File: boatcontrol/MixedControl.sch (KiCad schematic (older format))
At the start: 12 parts, among them J21 Conn_01x01_Male, J22 Conn_01x01_Male, J23 Conn_02x20_Odd_Even Socket, U15 MCP23017-E/SP

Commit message: Fixed I2C addresses
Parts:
- removed JP16, JP17, JP18: SolderJumper_3_Open, Jumper:SolderJumper-3_P1.3mm_Open_RoundedPad1.0x1.5mm_NumberLabels, symbol Jumper:SolderJumper_3_Open
- added JP16, JP17, JP18: SolderJumper_3_Bridged12, symbol Jumper:SolderJumper_3_Bridged12
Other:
- note added: "I2C Address 0x24"
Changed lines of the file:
@@
 	3250 4450 2950 4450
-$Comp
-L Jumper:SolderJumper_3_Open JP?
-U 1 1 E142CC81
-P 2950 4300
-AR Path="/E142CC81" Ref="JP?"  Part="1"
-AR Path="/D16552B4/E142CC81" Ref="JP?"  Part="1"
-AR Path="/D1BB8DB4/E142CC81" Ref="JP?"  Part="1"
-AR Path="/E0EE2714/E1383403/E142CC81" Ref="JP?"  Part="1"
-AR Path="/E171B33C/E142CC81" Ref="JP18"  Part="1"
-F 0 "JP18" H 2950 4400 50  0000 C CNN
-F 1 "SolderJumper_3_Open" V 2800 4750 50  0001 C CNN
-F 2 "Jumper:SolderJumper-3_P1.3mm_Open_RoundedPad1.0x1.5mm_NumberLabels" H 2950 4300 50  0001 C CNN
-F 3 "~" H 2950 4300 50  0001 C CNN
-	1    2950 4300
-	1    0    0    -1
-$EndComp
-$Comp
-L Jumper:SolderJumper_3_Open JP?
-U 1 1 E142CC87
-P 2400 4400
-AR Path="/E142CC87" Ref="JP?"  Part="1"
-AR Path="/D16552B4/E142CC87" Ref="JP?"  Part="1"
-AR Path="/D1BB8DB4/E142CC87" Ref="JP?"  Part="1"
-AR Path="/E0EE2714/E1383403/E142CC87" Ref="JP?"  Part="1"
-AR Path="/E171B33C/E142CC87" Ref="JP17"  Part="1"
-F 0 "JP17" H 2400 4500 50  0000 C CNN
-F 1 "SolderJumper_3_Open" V 2250 4850 50  0001 C CNN
-F 2 "Jumper:SolderJumper-3_P1.3mm_Open_RoundedPad1.0x1.5mm_NumberLabels" H 2400 4400 50  0001 C CNN
-F 3 "~" H 2400 4400 50  0001 C CNN
-	1    2400 4400
-	1    0    0    -1
-$EndComp
-$Comp
-L Jumper:SolderJumper_3_Open JP?
-U 1 1 E142CC8D
-P 1900 4500
-AR Path="/E142CC8D" Ref="JP?"  Part="1"
-AR Path="/D16552B4/E142CC8D" Ref="JP?"  Part="1"
-AR Path="/D1BB8DB4/E142CC8D" Ref="JP?"  Part="1"
-AR Path="/E0EE2714/E1383403/E142CC8D" Ref="JP?"  Part="1"
-AR Path="/E171B33C/E142CC8D" Ref="JP16"  Part="1"
-F 0 "JP16" H 1900 4600 50  0000 C CNN
-F 1 "SolderJumper_3_Open" V 1750 4950 50  0001 C CNN
-F 2 "Jumper:SolderJumper-3_P1.3mm_Open_RoundedPad1.0x1.5mm_NumberLabels" H 1900 4500 50  0001 C CNN
-F 3 "~" H 1900 4500 50  0001 C CNN
-	1    1900 4500
-	1    0    0    -1
-$EndComp
 $Comp
 L Connector:Conn_01x01_Male J?
@@
 Wire Wire Line
 	2600 4950 3150 4950
-Wire Wire Line
-	1700 2750 1700 4500
 Wire Wire Line
 	2100 4500 2100 4950
@@
 Wire Wire Line
 	3250 3950 3100 3950
-Connection ~ 3050 4100
+Text Notes 3700 4050 3    50   ~ 0
+I2C Address 0x24
+$Comp
+L Jumper:SolderJumper_3_Bridged12 JP?
+U 1 1 5F735A80
+P 2950 4300
+AR Path="/5F735A80" Ref="JP?"  Part="1"
+AR Path="/D16552B4/5F735A80" Ref="JP?"  Part="1"
+AR Path="/E171B33C/5F735A80" Ref="JP18"  Part="1"
+F 0 "JP18" H 2950 4413 50  0000 C CNN
+F 1 "SolderJumper_3_Bridged12" H 2950 4414 50  0001 C CNN
+F 2 "" H 2950 4300 50  0001 C CNN
+F 3 "~" H 2950 4300 50  0001 C CNN
+	1    2950 4300
+	1    0    0    -1
+$EndComp
+$Comp
+L Jumper:SolderJumper_3_Bridged12 JP?
+U 1 1 5F735A8C
+P 1900 4500
+AR Path="/5F735A8C" Ref="JP?"  Part="1"
+AR Path="/D16552B4/5F735A8C" Ref="JP?"  Part="1"
+AR Path="/E171B33C/5F735A8C" Ref="JP16"  Part="1"
+F 0 "JP16" H 1900 4613 50  0000 C CNN
+F 1 "SolderJumper_3_Bridged12" H 1900 4614 50  0001 C CNN
+F 2 "" H 1900 4500 50  0001 C CNN
+F 3 "~" H 1900 4500 50  0001 C CNN
+	1    1900 4500
+	-1   0    0    -1
+$EndComp
+$Comp
+L Jumper:SolderJumper_3_Bridged12 JP?
+U 1 1 5F74DFEC
+P 2400 4400
+AR Path="/5F74DFEC" Ref="JP?"  Part="1"
+AR Path="/D16552B4/5F74DFEC" Ref="JP?"  Part="1"
+AR Path="/E171B33C/5F74DFEC" Ref="JP17"  Part="1"
+F 0 "JP17" H 2400 4513 50  0000 C CNN
+F 1 "SolderJumper_3_Bridged12" H 2400 4514 50  0001 C CNN
+F 2 "" H 2400 4400 50  0001 C CNN
+F 3 "~" H 2400 4400 50  0001 C CNN
+	1    2400 4400
+	-1   0    0    -1
+$EndComp
+Wire Wire Line
+	1700 2750 1700 4500
 $EndSCHEMATC

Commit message: Fixed SolderJumpers
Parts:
- JP16, JP17, JP18: footprint (none) -> Jumper:SolderJumper-3_P1.3mm_Bridged12_RoundedPad1.0x1.5mm; symbol Jumper:SolderJumper_3_Bridged12 -> Jumper:SolderJumper_3_Bridged12_Output
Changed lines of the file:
@@
 I2C Address 0x24
 $Comp
-L Jumper:SolderJumper_3_Bridged12 JP?
+L Jumper:SolderJumper_3_Bridged12_Output JP?
 U 1 1 5F735A80
 P 2950 4300
@@
 F 0 "JP18" H 2950 4413 50  0000 C CNN
 F 1 "SolderJumper_3_Bridged12" H 2950 4414 50  0001 C CNN
-F 2 "" H 2950 4300 50  0001 C CNN
+F 2 "Jumper:SolderJumper-3_P1.3mm_Bridged12_RoundedPad1.0x1.5mm" H 2950 4300 50  0001 C CNN
 F 3 "~" H 2950 4300 50  0001 C CNN
 	1    2950 4300
@@
 $EndComp
 $Comp
-L Jumper:SolderJumper_3_Bridged12 JP?
+L Jumper:SolderJumper_3_Bridged12_Output JP?
 U 1 1 5F735A8C
 P 1900 4500
@@
 F 0 "JP16" H 1900 4613 50  0000 C CNN
 F 1 "SolderJumper_3_Bridged12" H 1900 4614 50  0001 C CNN
-F 2 "" H 1900 4500 50  0001 C CNN
+F 2 "Jumper:SolderJumper-3_P1.3mm_Bridged12_RoundedPad1.0x1.5mm" H 1900 4500 50  0001 C CNN
 F 3 "~" H 1900 4500 50  0001 C CNN
 	1    1900 4500
@@
 $EndComp
 $Comp
-L Jumper:SolderJumper_3_Bridged12 JP?
+L Jumper:SolderJumper_3_Bridged12_Output JP?
 U 1 1 5F74DFEC
 P 2400 4400
@@
 F 0 "JP17" H 2400 4513 50  0000 C CNN
 F 1 "SolderJumper_3_Bridged12" H 2400 4514 50  0001 C CNN
-F 2 "" H 2400 4400 50  0001 C CNN
+F 2 "Jumper:SolderJumper-3_P1.3mm_Bridged12_RoundedPad1.0x1.5mm" H 2400 4400 50  0001 C CNN
 F 3 "~" H 2400 4400 50  0001 C CNN
 	1    2400 4400

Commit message: Before starting the PCB fresh
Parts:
- renumbered H27 to H2401, H28 to H2402, H29 to H2403, H30 to H2404, J21 to J2401, J22 to J2402, J23 to J2403, JP16 to JP2401, JP17 to JP2402, JP18 to JP2403, JP19 to JP2404, U15 to U2401
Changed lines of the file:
@@
 AR Path="/D1BB8DB4/E142CB7C" Ref="U?"  Part="1"
 AR Path="/E0EE2714/E1383403/E142CB7C" Ref="U?"  Part="1"
-AR Path="/E171B33C/E142CB7C" Ref="U15"  Part="1"
-F 0 "U15" V 4000 3750 50  0000 L CNN
+AR Path="/E171B33C/E142CB7C" Ref="U2401"  Part="1"
+F 0 "U2401" V 4000 3750 50  0000 L CNN
 F 1 "MCP23017-E/SP" V 3900 3550 50  0000 L CNN
 F 2 "Package_DIP:DIP-28_W7.62mm" H 4150 2850 50  0001 L CNN
@@
 AR Path="/D1BB8DB4/E142CC74" Ref="JP?"  Part="1"
 AR Path="/E0EE2714/E1383403/E142CC74" Ref="JP?"  Part="1"
-AR Path="/E171B33C/E142CC74" Ref="JP19"  Part="1"
-F 0 "JP19" H 3000 4050 50  0000 C CNN
+AR Path="/E171B33C/E142CC74" Ref="JP2404"  Part="1"
+F 0 "JP2404" H 3000 4050 50  0000 C CNN
 F 1 "Jumper_NO_Small" H 3050 3850 50  0001 C CNN
 F 2 "Connector_PinHeader_2.54mm:PinHeader_1x02_P2.54mm_Vertical" H 3000 3950 50  0001 C CNN
@@
 AR Path="/D1BB8DB4/E142CC7A" Ref="J?"  Part="1"
 AR Path="/E0EE2714/E1383403/E142CC7A" Ref="J?"  Part="1"
-AR Path="/E171B33C/E142CC7A" Ref="J22"  Part="1"
-F 0 "J22" H 2950 3800 50  0000 R CNN
+AR Path="/E171B33C/E142CC7A" Ref="J2402"  Part="1"
+F 0 "J2402" H 2950 3800 50  0000 R CNN
 F 1 "Conn_01x01_Male" H 2872 3773 50  0001 R CNN
 F 2 "Connector_PinHeader_2.54mm:PinHeader_1x01_P2.54mm_Vertical" H 2900 3750 50  0001 C CNN
@@
 AR Path="/D1BB8DB4/E142CC93" Ref="J?"  Part="1"
 AR Path="/E0EE2714/E1383403/E142CC93" Ref="J?"  Part="1"
-AR Path="/E171B33C/E142CC93" Ref="J21"  Part="1"
-F 0 "J21" H 2950 3700 50  0000 R CNN
+AR Path="/E171B33C/E142CC93" Ref="J2401"  Part="1"
+F 0 "J2401" H 2950 3700 50  0000 R CNN
 F 1 "Conn_01x01_Male" H 2872 3673 50  0001 R CNN
 F 2 "Connector_PinHeader_2.54mm:PinHeader_1x01_P2.54mm_Vertical" H 2900 3650 50  0001 C CNN
@@
 AR Path="/D1BB8DB4/E142CCB8" Ref="#PWR?"  Part="1"
 AR Path="/E0EE2714/E1383403/E142CCB8" Ref="#PWR?"  Part="1"
-AR Path="/E171B33C/E142CCB8" Ref="#PWR081"  Part="1"
-F 0 "#PWR081" H 3950 4700 50  0001 C CNN
+AR Path="/E171B33C/E142CCB8" Ref="#PWR02402"  Part="1"
+F 0 "#PWR02402" H 3950 4700 50  0001 C CNN
 F 1 "GND" H 4100 4900 50  0000 C CNN
 F 2 "" H 3950 4950 50  0001 C CNN
@@
 AR Path="/D1BB8DB4/E142CCC5" Ref="#PWR?"  Part="1"
 AR Path="/E0EE2714/E1383403/E142CCC5" Ref="#PWR?"  Part="1"
-AR Path="/E171B33C/E142CCC5" Ref="#PWR080"  Part="1"
-F 0 "#PWR080" H 3950 2600 50  0001 C CNN
+AR Path="/E171B33C/E142CCC5" Ref="#PWR02401"  Part="1"
+F 0 "#PWR02401" H 3950 2600 50  0001 C CNN
 F 1 "+5V" H 4100 2800 50  0000 C CNN
 F 2 "" H 3950 2750 50  0001 C CNN
@@
 AR Path="/E0EE2714/E15696A6" Ref="H?"  Part="1"
 AR Path="/E0EE2714/E1383403/E15696A6" Ref="H?"  Part="1"
-AR Path="/E171B33C/E15696A6" Ref="H29"  Part="1"
-F 0 "H29" H 9700 3800 50  0000 L CNN
+AR Path="/E171B33C/E15696A6" Ref="H2403"  Part="1"
+F 0 "H2403" H 9700 3800 50  0000 L CNN
 F 1 "MountingHole" V 9750 3750 50  0001 L CNN
 F 2 "MountingHole:MountingHole_3mm" H 9750 3650 50  0001 C CNN
@@
 AR Path="/E0EE2714/E15696A0" Ref="H?"  Part="1"
 AR Path="/E0EE2714/E1383403/E15696A0" Ref="H?"  Part="1"
-AR Path="/E171B33C/E15696A0" Ref="H30"  Part="1"
-F 0 "H30" H 9700 3850 50  0000 L CNN
+AR Path="/E171B33C/E15696A0" Ref="H2404"  Part="1"
+F 0 "H2404" H 9700 3850 50  0000 L CNN
 F 1 "MountingHole" H 9850 3955 50  0001 L CNN
 F 2 "MountingHole:MountingHole_3mm" H 9750 4000 50  0001 C CNN
@@
 AR Path="/E0EE2714/E156969A" Ref="J?"  Part="1"
 AR Path="/E0EE2714/E1383403/E156969A" Ref="J?"  Part="1"
-AR Path="/E171B33C/E156969A" Ref="J23"  Part="1"
-F 0 "J23" V 8600 4900 50  0000 R CNN
+AR Path="/E171B33C/E156969A" Ref="J2403"  Part="1"
+F 0 "J2403" V 8600 4900 50  0000 R CNN
 F 1 "Conn_02x20_Odd_Even Socket" V 8600 4200 50  0000 R CNN
 F 2 "Connector_PinHeader_2.54mm:PinHeader_2x20_P2.54mm_Vertical" H 8550 3800 50  0001 C CNN
@@
 AR Path="/E0EE2714/E15696AC" Ref="H?"  Part="1"
 AR Path="/E0EE2714/E1383403/E15696AC" Ref="H?"  Part="1"
-AR Path="/E171B33C/E15696AC" Ref="H27"  Part="1"
-F 0 "H27" V 7600 3600 50  0000 L CNN
+AR Path="/E171B33C/E15696AC" Ref="H2401"  Part="1"
+F 0 "H2401" V 7600 3600 50  0000 L CNN
 F 1 "MountingHole" H 7550 3605 50  0001 L CNN
 F 2 "MountingHole:MountingHole_3mm" H 7450 3650 50  0001 C CNN
@@
 AR Path="/E0EE2714/E15696B2" Ref="H?"  Part="1"
 AR Path="/E0EE2714/E1383403/E15696B2" Ref="H?"  Part="1"
-AR Path="/E171B33C/E15696B2" Ref="H28"  Part="1"
-F 0 "H28" V 7300 3950 50  0000 L CNN
+AR Path="/E171B33C/E15696B2" Ref="H2402"  Part="1"
+F 0 "H2402" V 7300 3950 50  0000 L CNN
 F 1 "MountingHole" H 7550 3955 50  0001 L CNN
 F 2 "MountingHole:MountingHole_3mm" H 7450 4000 50  0001 C CNN
@@
 P 9650 3850
 AR Path="/E0EE2714/E1383403/E16C27B4" Ref="#PWR?"  Part="1"
-AR Path="/E171B33C/E16C27B4" Ref="#PWR082"  Part="1"
-F 0 "#PWR082" H 9650 3600 50  0001 C CNN
+AR Path="/E171B33C/E16C27B4" Ref="#PWR02403"  Part="1"
+F 0 "#PWR02403" H 9650 3600 50  0001 C CNN
 F 1 "GND" V 9650 3750 50  0000 R CNN
 F 2 "" H 9650 3850 50  0001 C CNN
@@
 AR Path="/5F735A80" Ref="JP?"  Part="1"
 AR Path="/D16552B4/5F735A80" Ref="JP?"  Part="1"
-AR Path="/E171B33C/5F735A80" Ref="JP18"  Part="1"
-F 0 "JP18" H 2950 4413 50  0000 C CNN
+AR Path="/E171B33C/5F735A80" Ref="JP2403"  Part="1"
+F 0 "JP2403" H 2950 4413 50  0000 C CNN
 F 1 "SolderJumper_3_Bridged12" H 2950 4414 50  0001 C CNN
 F 2 "Jumper:SolderJumper-3_P1.3mm_Bridged12_RoundedPad1.0x1.5mm" H 2950 4300 50  0001 C CNN
@@
 AR Path="/5F735A8C" Ref="JP?"  Part="1"
 AR Path="/D16552B4/5F735A8C" Ref="JP?"  Part="1"
-AR Path="/E171B33C/5F735A8C" Ref="JP16"  Part="1"
-F 0 "JP16" H 1900 4613 50  0000 C CNN
+AR Path="/E171B33C/5F735A8C" Ref="JP2401"  Part="1"
+F 0 "JP2401" H 1900 4613 50  0000 C CNN
 F 1 "SolderJumper_3_Bridged12" H 1900 4614 50  0001 C CNN
 F 2 "Jumper:SolderJumper-3_P1.3mm_Bridged12_RoundedPad1.0x1.5mm" H 1900 4500 50  0001 C CNN
@@
 AR Path="/5F74DFEC" Ref="JP?"  Part="1"
 AR Path="/D16552B4/5F74DFEC" Ref="JP?"  Part="1"
-AR Path="/E171B33C/5F74DFEC" Ref="JP17"  Part="1"
-F 0 "JP17" H 2400 4513 50  0000 C CNN
+AR Path="/E171B33C/5F74DFEC" Ref="JP2402"  Part="1"
+F 0 "JP2402" H 2400 4513 50  0000 C CNN
 F 1 "SolderJumper_3_Bridged12" H 2400 4514 50  0001 C CNN
 F 2 "Jumper:SolderJumper-3_P1.3mm_Bridged12_RoundedPad1.0x1.5mm" H 2400 4400 50  0001 C CNN

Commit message: Structured
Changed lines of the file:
@@
 $Descr A4 11693 8268
 encoding utf-8
-Sheet 24 55
+Sheet 23 55
 Title "Boat Control Hat"
 Date "2020-07-09"
@@
 Wire Wire Line
 	1700 2750 1700 4500
+$Sheet
+S 5650 3750 1350 150
+U 5F80BAC6
+F0 "Relay Board" 50
+F1 "RelayBoard.sch" 50
+$EndSheet
 $EndSCHEMATC

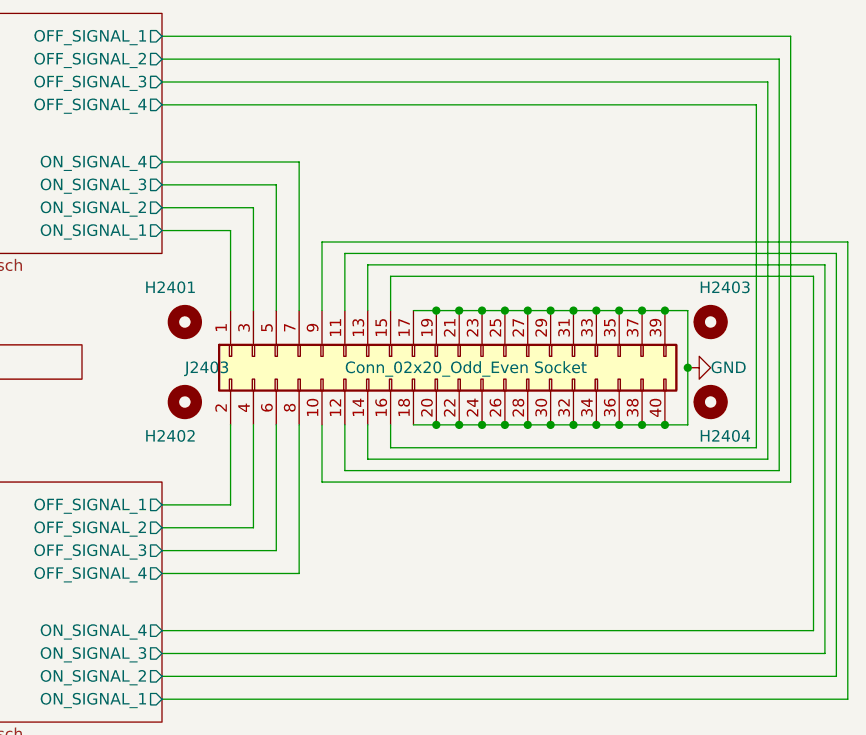
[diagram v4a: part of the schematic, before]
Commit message: Fixed daughter board
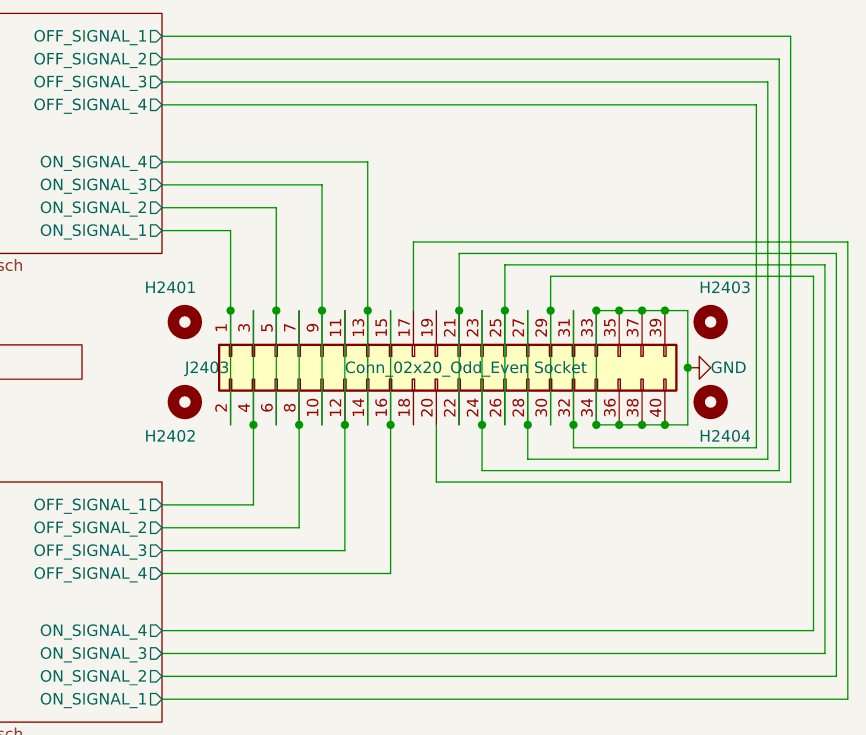
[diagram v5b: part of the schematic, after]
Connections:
- net GND: no longer J2403.17 (Pin_17), J2403.18 (Pin_18), J2403.19 (Pin_19), J2403.20 (Pin_20), J2403.21 (Pin_21), J2403.22 (Pin_22), J2403.23 (Pin_23), J2403.24 (Pin_24), J2403.25 (Pin_25), J2403.26 (Pin_26), J2403.27 (Pin_27), J2403.28 (Pin_28), J2403.29 (Pin_29), J2403.30 (Pin_30), J2403.31 (Pin_31), J2403.32 (Pin_32)
- net MixedBlock1/OFF_SIGNAL_1: now also J2403.20 (Pin_20); no longer J2403.10 (Pin_10)
- net MixedBlock1/OFF_SIGNAL_2: now also J2403.23 (Pin_23), J2403.24 (Pin_24); no longer J2403.12 (Pin_12)
- net MixedBlock1/OFF_SIGNAL_3: now also J2403.27 (Pin_27), J2403.28 (Pin_28); no longer J2403.14 (Pin_14)
- net MixedBlock1/OFF_SIGNAL_4: now also J2403.31 (Pin_31), J2403.32 (Pin_32); no longer J2403.16 (Pin_16)
- net MixedBlock1/ON_SIGNAL_1: now also J2403.2 (Pin_2)
- net MixedBlock1/ON_SIGNAL_2: now also J2403.5 (Pin_5), J2403.6 (Pin_6); no longer J2403.3 (Pin_3)
- net MixedBlock1/ON_SIGNAL_3: now also J2403.10 (Pin_10), J2403.9 (Pin_9); no longer J2403.5 (Pin_5)
- net MixedBlock1/ON_SIGNAL_4: now also J2403.13 (Pin_13), J2403.14 (Pin_14); no longer J2403.7 (Pin_7)
- net MixedBlock2/OFF_SIGNAL_1: now also J2403.3 (Pin_3), J2403.4 (Pin_4); no longer J2403.2 (Pin_2)
- net MixedBlock2/OFF_SIGNAL_2: now also J2403.7 (Pin_7), J2403.8 (Pin_8); no longer J2403.4 (Pin_4)
- net MixedBlock2/OFF_SIGNAL_3: now also J2403.11 (Pin_11), J2403.12 (Pin_12); no longer J2403.6 (Pin_6)
- net MixedBlock2/OFF_SIGNAL_4: now also J2403.15 (Pin_15), J2403.16 (Pin_16); no longer J2403.8 (Pin_8)
- net MixedBlock2/ON_SIGNAL_1: now also J2403.17 (Pin_17); no longer J2403.9 (Pin_9)
- net MixedBlock2/ON_SIGNAL_2: now also J2403.21 (Pin_21), J2403.22 (Pin_22); no longer J2403.11 (Pin_11)
- net MixedBlock2/ON_SIGNAL_3: now also J2403.25 (Pin_25), J2403.26 (Pin_26); no longer J2403.13 (Pin_13)
- net MixedBlock2/ON_SIGNAL_4: now also J2403.29 (Pin_29), J2403.30 (Pin_30); no longer J2403.15 (Pin_15)
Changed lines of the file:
@@
 	4650 4650 4650 5300
 Wire Wire Line
-	8350 4200 8350 4100
-Wire Wire Line
-	8250 4250 8250 4100
-Wire Wire Line
-	8150 4300 8150 4100
-Wire Wire Line
-	8050 4350 8050 4100
-Wire Wire Line
-	8350 3600 8350 3450
-Wire Wire Line
-	7350 2950 7950 2950
-Wire Wire Line
-	7950 2950 7950 3600
-Wire Wire Line
-	7350 3050 7850 3050
-Wire Wire Line
-	7850 3050 7850 3600
-Wire Wire Line
-	7350 3150 7750 3150
-Wire Wire Line
-	7750 3150 7750 3600
-Wire Wire Line
 	7650 3250 7650 3600
 Wire Wire Line
 	7350 3250 7650 3250
 Wire Wire Line
-	8250 3400 8250 3600
-Wire Wire Line
-	8150 3350 8150 3600
-Wire Wire Line
-	8050 3300 8050 3600
-Wire Wire Line
-	7350 4750 7950 4750
-Wire Wire Line
-	7950 4750 7950 4100
-Wire Wire Line
-	7350 4650 7850 4650
-Wire Wire Line
-	7850 4650 7850 4100
-Wire Wire Line
-	7350 4550 7750 4550
-Wire Wire Line
-	7750 4550 7750 4100
-Wire Wire Line
-	7350 4450 7650 4450
-Wire Wire Line
-	7650 4450 7650 4100
-Wire Wire Line
-	8450 3600 8550 3600
-Connection ~ 8550 3600
-Wire Wire Line
-	8550 3600 8650 3600
-Connection ~ 8650 3600
-Wire Wire Line
-	8650 3600 8750 3600
-Connection ~ 8750 3600
-Wire Wire Line
-	8750 3600 8850 3600
-Connection ~ 8850 3600
-Wire Wire Line
-	8850 3600 8950 3600
-Connection ~ 8950 3600
-Wire Wire Line
-	8950 3600 9050 3600
-Connection ~ 9050 3600
-Wire Wire Line
-	9050 3600 9150 3600
-Connection ~ 9150 3600
-Wire Wire Line
-	9150 3600 9250 3600
-Connection ~ 9250 3600
-Wire Wire Line
-	9250 3600 9350 3600
-Connection ~ 9350 3600
-Wire Wire Line
-	9350 3600 9450 3600
-Connection ~ 9450 3600
-Wire Wire Line
-	9450 3600 9550 3600
-Wire Wire Line
-	8550 4100 8650 4100
-Connection ~ 8650 4100
-Wire Wire Line
-	8650 4100 8750 4100
-Connection ~ 8750 4100
-Wire Wire Line
-	8750 4100 8850 4100
-Connection ~ 8850 4100
-Wire Wire Line
-	8850 4100 8950 4100
-Connection ~ 8950 4100
-Wire Wire Line
-	8950 4100 9050 4100
-Connection ~ 9050 4100
-Wire Wire Line
-	9050 4100 9150 4100
-Connection ~ 9150 4100
-Wire Wire Line
-	9150 4100 9250 4100
-Connection ~ 9250 4100
-Wire Wire Line
-	9250 4100 9350 4100
-Connection ~ 9350 4100
-Wire Wire Line
-	9350 4100 9450 4100
-Connection ~ 9450 4100
-Wire Wire Line
-	9450 4100 9550 4100
-Connection ~ 9550 3600
-Wire Wire Line
 	9650 3600 9650 3850
-Wire Wire Line
-	9650 4100 9550 4100
-Connection ~ 9550 4100
-Wire Wire Line
-	9550 3600 9650 3600
 $Comp
 L power:GND #PWR?
@@
 	10350 3300 10350 5300
 Wire Wire Line
-	8050 3300 10350 3300
-Wire Wire Line
 	7350 5300 10350 5300
 Wire Wire Line
 	10300 3350 10300 5200
 Wire Wire Line
-	8150 3350 10300 3350
-Wire Wire Line
 	7350 5200 10300 5200
 Wire Wire Line
@@
 	10200 3450 10200 5000
 Wire Wire Line
-	8350 3450 10200 3450
-Wire Wire Line
 	7350 5000 10200 5000
 Wire Wire Line
-	8250 3400 10250 3400
-Wire Wire Line
 	10100 4350 10100 2400
 Wire Wire Line
 	7350 2400 10100 2400
 Wire Wire Line
-	8050 4350 10100 4350
-Wire Wire Line
 	10050 4300 10050 2500
 Wire Wire Line
 	7350 2500 10050 2500
 Wire Wire Line
-	8150 4300 10050 4300
-Wire Wire Line
 	10000 4250 10000 2600
 Wire Wire Line
 	7350 2600 10000 2600
 Wire Wire Line
-	8250 4250 10000 4250
-Wire Wire Line
 	9950 2700 9950 4200
 Wire Wire Line
 	7350 2700 9950 2700
-Wire Wire Line
-	8350 4200 9950 4200
 Text GLabel 4850 2400 2    50   Input ~ 0
 IND_C1_ON
@@
 SCK
 Wire Wire Line
-	8550 4100 8450 4100
-Connection ~ 8550 4100
-Wire Wire Line
 	3250 3950 3100 3950
 Text Notes 3700 4050 3    50   ~ 0
@@
 F1 "RelayBoard.sch" 50
 $EndSheet
+Wire Wire Line
+	9650 3600 9550 3600
+Wire Wire Line
+	9650 4100 9550 4100
+Wire Wire Line
+	9550 3600 9450 3600
+Wire Wire Line
+	9250 3600 9250 4100
+Connection ~ 9550 3600
+Connection ~ 9250 3600
+Connection ~ 9350 3600
+Wire Wire Line
+	9350 3600 9250 3600
+Connection ~ 9450 3600
+Wire Wire Line
+	9450 3600 9350 3600
+Wire Wire Line
+	9550 4100 9450 4100
+Connection ~ 9550 4100
+Connection ~ 9250 4100
+Connection ~ 9350 4100
+Wire Wire Line
+	9350 4100 9250 4100
+Connection ~ 9450 4100
+Wire Wire Line
+	9450 4100 9350 4100
+Wire Wire Line
+	9150 4100 9150 4200
+Wire Wire Line
+	9150 4200 9950 4200
+Wire Wire Line
+	9150 4100 9150 3600
+Connection ~ 9150 4100
+Wire Wire Line
+	9050 3600 9050 3450
+Wire Wire Line
+	9050 3450 10200 3450
+Wire Wire Line
+	9050 3600 9050 4100
+Connection ~ 9050 3600
+Wire Wire Line
+	8950 4250 8950 4100
+Wire Wire Line
+	8950 4250 10000 4250
+Wire Wire Line
+	8950 4100 8950 3600
+Connection ~ 8950 4100
+Wire Wire Line
+	8850 3400 8850 3600
+Wire Wire Line
+	8850 3400 10250 3400
+Wire Wire Line
+	8850 3600 8850 4100
+Connection ~ 8850 3600
+Wire Wire Line
+	8750 4300 8750 4100
+Wire Wire Line
+	8750 4300 10050 4300
+Wire Wire Line
+	8750 4100 8750 3600
+Connection ~ 8750 4100
+Wire Wire Line
+	8650 3350 8650 3600
+Wire Wire Line
+	8650 3600 8650 4100
+Wire Wire Line
+	8650 3350 10300 3350
+Connection ~ 8650 3600
+Wire Wire Line
+	8550 4350 8550 4100
+Wire Wire Line
+	8550 4350 10100 4350
+Wire Wire Line
+	8450 3300 8450 3600
+Wire Wire Line
+	8450 3300 10350 3300
+Wire Wire Line
+	8350 4750 8350 4100
+Wire Wire Line
+	8350 4100 8350 3600
+Connection ~ 8350 4100
+Wire Wire Line
+	7350 4750 8350 4750
+Wire Wire Line
+	8250 2950 8250 3600
+Wire Wire Line
+	8250 3600 8250 4100
+Connection ~ 8250 3600
+Wire Wire Line
+	7350 2950 8250 2950
+Wire Wire Line
+	8150 4650 8150 4100
+Wire Wire Line
+	8150 4100 8150 3600
+Connection ~ 8150 4100
+Wire Wire Line
+	7350 4650 8150 4650
+Wire Wire Line
+	8050 3050 8050 3600
+Wire Wire Line
+	8050 3600 8050 4100
+Connection ~ 8050 3600
+Wire Wire Line
+	7350 3050 8050 3050
+Wire Wire Line
+	7950 4550 7950 4100
+Wire Wire Line
+	7950 4100 7950 3600
+Connection ~ 7950 4100
+Wire Wire Line
+	7350 4550 7950 4550
+Wire Wire Line
+	7850 3150 7850 3600
+Wire Wire Line
+	7850 3600 7850 4100
+Connection ~ 7850 3600
+Wire Wire Line
+	7350 3150 7850 3150
+Wire Wire Line
+	7750 4450 7750 4100
+Wire Wire Line
+	7350 4450 7750 4450
+Wire Wire Line
+	7750 4100 7750 3600
+Connection ~ 7750 4100
+Wire Wire Line
+	7650 3600 7650 4100
+Connection ~ 7650 3600
 $EndSCHEMATC

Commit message: interrim
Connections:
- net MixedBlock1/OFF_SIGNAL_1: now also J2403.19 (Pin_19)
- net MixedBlock2/ON_SIGNAL_1: now also J2403.18 (Pin_18)
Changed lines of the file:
@@
 	7650 3600 7650 4100
 Connection ~ 7650 3600
+Wire Wire Line
+	8450 4100 8450 3600
+Connection ~ 8450 3600
+Wire Wire Line
+	8550 3600 8550 4100
+Connection ~ 8550 4100
 $EndSCHEMATC
